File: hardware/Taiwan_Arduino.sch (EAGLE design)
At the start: 43 parts, among them J1 AVR_SPI_PRG_62X3_LOCK, T2 2N2222, U1 ATMEGA328P_PDIP, U2 SPI_FLASH, Y2 16mhz

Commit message: add FTDI Tag
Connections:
- net GND: now also S1.2; no longer S1.1
- net RST: now also S1.1; no longer S1.2
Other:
- moved on the sheet: S1
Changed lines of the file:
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@@
 <?xml version="1.0" encoding="utf-8"?>
 <!DOCTYPE eagle SYSTEM "eagle.dtd">
-<eagle version="7.2.0">
+<eagle version="7.4.0">
 <drawing>
 <settings>
@@
 <grid distance="0.1" unitdist="inch" unit="inch" style="lines" multiple="1" display="no" altdistance="0.01" altunitdist="inch" altunit="inch"/>
 <layers>
-<layer number="1" name="Top" color="4" fill="1" visible="yes" active="no"/>
-<layer number="16" name="Bottom" color="1" fill="1" visible="yes" active="no"/>
-<layer number="17" name="Pads" color="2" fill="1" visible="yes" active="no"/>
-<layer number="18" name="Vias" color="2" fill="1" visible="yes" active="no"/>
-<layer number="19" name="Unrouted" color="6" fill="1" visible="yes" active="no"/>
-<layer number="20" name="Dimension" color="15" fill="1" visible="yes" active="no"/>
-<layer number="21" name="tPlace" color="7" fill="1" visible="yes" active="no"/>
-<layer number="22" name="bPlace" color="7" fill="1" visible="yes" active="no"/>
-<layer number="23" name="tOrigins" color="15" fill="1" visible="yes" active="no"/>
-<layer number="24" name="bOrigins" color="15" fill="1" visible="yes" active="no"/>
-<layer number="25" name="tNames" color="7" fill="1" visible="yes" active="no"/>
-<layer number="26" name="bNames" color="7" fill="1" visible="yes" active="no"/>
-<layer number="27" name="tValues" color="7" fill="1" visible="yes" active="no"/>
-<layer number="28" name="bValues" color="7" fill="1" visible="yes" active="no"/>
+<layer number="1" name="Top" color="4" fill="1" visible="no" active="no"/>
+<layer number="16" name="Bottom" color="1" fill="1" visible="no" active="no"/>
+<layer number="17" name="Pads" color="2" fill="1" visible="no" active="no"/>
+<layer number="18" name="Vias" color="2" fill="1" visible="no" active="no"/>
+<layer number="19" name="Unrouted" color="6" fill="1" visible="no" active="no"/>
+<layer number="20" name="Dimension" color="15" fill="1" visible="no" active="no"/>
+<layer number="21" name="tPlace" color="7" fill="1" visible="no" active="no"/>
+<layer number="22" name="bPlace" color="7" fill="1" visible="no" active="no"/>
+<layer number="23" name="tOrigins" color="15" fill="1" visible="no" active="no"/>
+<layer number="24" name="bOrigins" color="15" fill="1" visible="no" active="no"/>
+<layer number="25" name="tNames" color="7" fill="1" visible="no" active="no"/>
+<layer number="26" name="bNames" color="7" fill="1" visible="no" active="no"/>
+<layer number="27" name="tValues" color="7" fill="1" visible="no" active="no"/>
+<layer number="28" name="bValues" color="7" fill="1" visible="no" active="no"/>
 <layer number="29" name="tStop" color="7" fill="3" visible="no" active="no"/>
 <layer number="30" name="bStop" color="7" fill="6" visible="no" active="no"/>
@@
 <layer number="35" name="tGlue" color="7" fill="4" visible="no" active="no"/>
 <layer number="36" name="bGlue" color="7" fill="5" visible="no" active="no"/>
-<layer number="37" name="tTest" color="7" fill="1" visible="yes" active="no"/>
-<layer number="38" name="bTest" color="7" fill="1" visible="yes" active="no"/>
+<layer number="37" name="tTest" color="7" fill="1" visible="no" active="no"/>
+<layer number="38" name="bTest" color="7" fill="1" visible="no" active="no"/>
 <layer number="39" name="tKeepout" color="4" fill="11" visible="no" active="no"/>
 <layer number="40" name="bKeepout" color="1" fill="11" visible="no" active="no"/>
@@
 <layer number="44" name="Drills" color="7" fill="1" visible="no" active="no"/>
 <layer number="45" name="Holes" color="7" fill="1" visible="no" active="no"/>
-<layer number="46" name="Milling" color="3" fill="1" visible="yes" active="no"/>
-<layer number="47" name="Measures" color="7" fill="1" visible="yes" active="no"/>
-<layer number="48" name="Document" color="7" fill="1" visible="yes" active="no"/>
-<layer number="49" name="Reference" color="7" fill="1" visible="yes" active="no"/>
-<layer number="50" name="dxf" color="7" fill="1" visible="yes" active="no"/>
-<layer number="51" name="tDocu" color="7" fill="1" visible="yes" active="no"/>
-<layer number="52" name="bDocu" color="7" fill="1" visible="yes" active="no"/>
-<layer number="53" name="tGND_GNDA" color="7" fill="9" visible="yes" active="no"/>
-<layer number="54" name="bGND_GNDA" color="1" fill="9" visible="yes" active="no"/>
-<layer number="56" name="wert" color="7" fill="1" visible="yes" active="no"/>
-<layer number="57" name="tCAD" color="7" fill="1" visible="yes" active="no"/>
-<layer number="59" name="tCarbon" color="7" fill="1" visible="yes" active="no"/>
-<layer number="60" name="bCarbon" color="7" fill="1" visible="yes" active="no"/>
+<layer number="46" name="Milling" color="3" fill="1" visible="no" active="no"/>
+<layer number="47" name="Measures" color="7" fill="1" visible="no" active="no"/>
+<layer number="48" name="Document" color="7" fill="1" visible="no" active="no"/>
+<layer number="49" name="Reference" color="7" fill="1" visible="no" active="no"/>
+<layer number="50" name="dxf" color="7" fill="1" visible="no" active="no"/>
+<layer number="51" name="tDocu" color="7" fill="1" visible="no" active="no"/>
+<layer number="52" name="bDocu" color="7" fill="1" visible="no" active="no"/>
+<layer number="53" name="tGND_GNDA" color="7" fill="9" visible="no" active="no"/>
+<layer number="54" name="bGND_GNDA" color="1" fill="9" visible="no" active="no"/>
+<layer number="56" name="wert" color="7" fill="1" visible="no" active="no"/>
+<layer number="57" name="tCAD" color="7" fill="1" visible="no" active="no"/>
+<layer number="59" name="tCarbon" color="7" fill="1" visible="no" active="no"/>
+<layer number="60" name="bCarbon" color="7" fill="1" visible="no" active="no"/>
 <layer number="90" name="Modules" color="5" fill="1" visible="yes" active="yes"/>
 <layer number="91" name="Nets" color="2" fill="1" visible="yes" active="yes"/>
@@
 <attribute name="VALUE" x="88.9" y="30.48" size="1.27" layer="96"/>
 </instance>
-<instance part="S1" gate="G$1" x="43.18" y="139.7" smashed="yes" rot="R180">
-<attribute name="NAME" x="43.18" y="142.24" size="1.778" layer="95" rot="R180"/>
-</instance>
-<instance part="GND7" gate="1" x="55.88" y="137.16"/>
+<instance part="S1" gate="G$1" x="43.18" y="139.7" smashed="yes">
+<attribute name="NAME" x="43.18" y="137.16" size="1.778" layer="95"/>
+</instance>
+<instance part="GND7" gate="1" x="48.26" y="137.16"/>
 <instance part="D1" gate="G$1" x="76.2" y="66.04" rot="R270"/>
 <instance part="R3" gate="G$1" x="66.04" y="66.04" rot="R180"/>
@@
 </segment>
 <segment>
-<pinref part="S1" gate="G$1" pin="1"/>
-<pinref part="GND7" gate="1" pin="GND"/>
-<wire x1="55.88" y1="139.7" x2="48.26" y2="139.7" width="0.1524" layer="91"/>
-</segment>
-<segment>
 <pinref part="GND12" gate="1" pin="GND"/>
 <pinref part="D5" gate="1" pin="A"/>
@@
 <pinref part="JP1" gate="G$1" pin="1"/>
 <wire x1="180.34" y1="81.28" x2="180.34" y2="73.66" width="0.1524" layer="91"/>
+</segment>
+<segment>
+<pinref part="S1" gate="G$1" pin="2"/>
+<pinref part="GND7" gate="1" pin="GND"/>
 </segment>
 </net>
@@
 <wire x1="38.1" y1="147.32" x2="139.7" y2="147.32" width="0.1524" layer="91"/>
 <wire x1="139.7" y1="147.32" x2="139.7" y2="116.84" width="0.1524" layer="91"/>
-<pinref part="S1" gate="G$1" pin="2"/>
 <wire x1="38.1" y1="147.32" x2="38.1" y2="139.7" width="0.1524" layer="91"/>
 <pinref part="U1" gate="G$1" pin="PC6(/RESET)"/>
@@
 <wire x1="38.1" y1="139.7" x2="38.1" y2="132.08" width="0.1524" layer="91"/>
 <wire x1="38.1" y1="139.7" x2="12.7" y2="139.7" width="0.1524" layer="91"/>
-</segment>
-</net>
+<pinref part="S1" gate="G$1" pin="1"/>
+<junction x="38.1" y="139.7"/>
+</segment>
+</net>

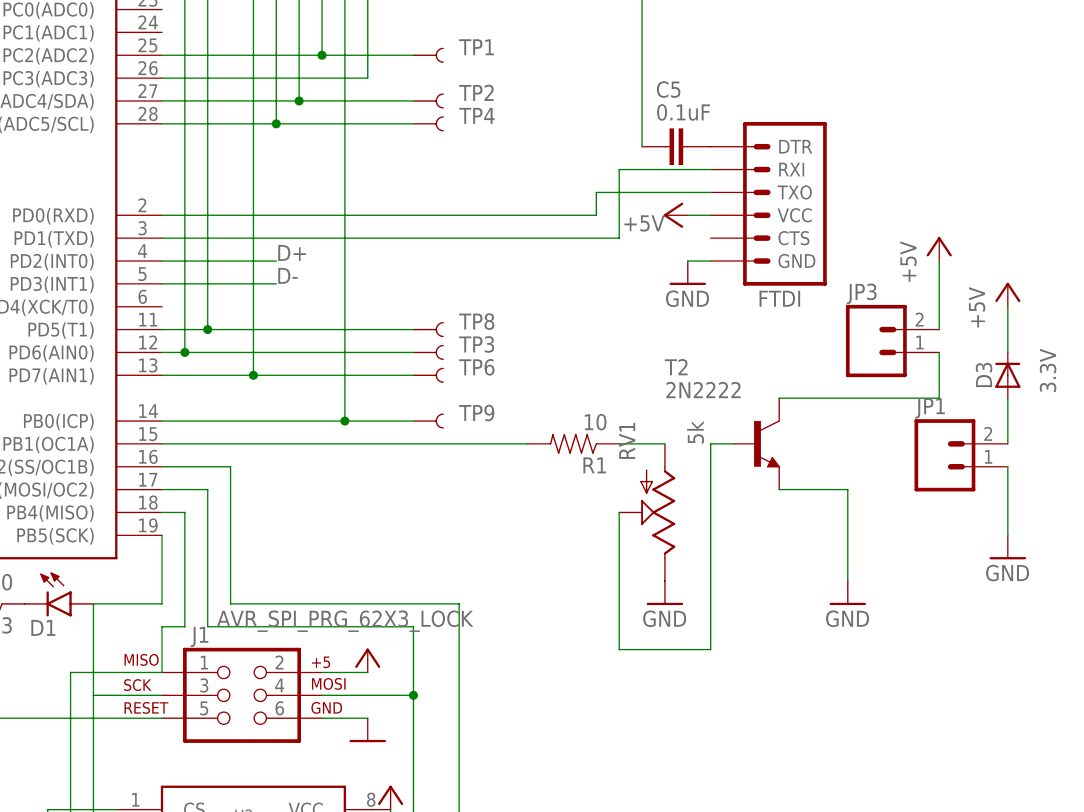
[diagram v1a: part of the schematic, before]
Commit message: Fix 10 ohm R1
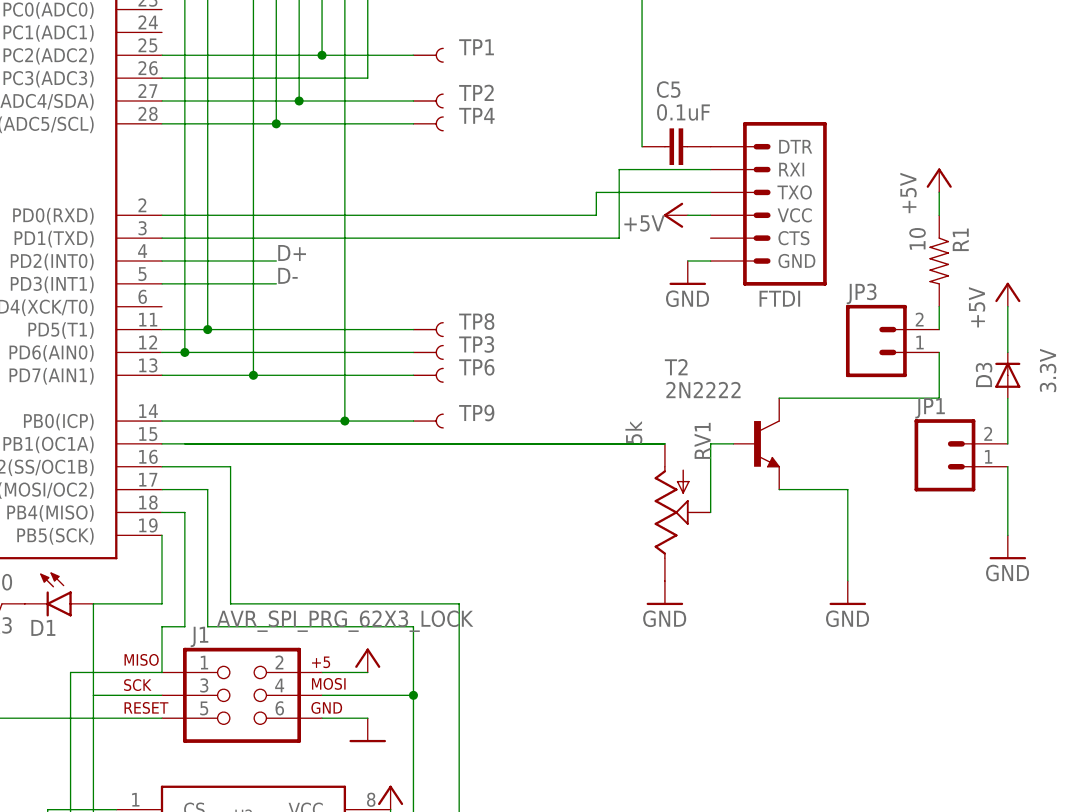
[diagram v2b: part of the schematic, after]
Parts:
- R1: device SparkFun-Resistors:RESISTORPTH-1/4W -> SparkFun-Resistors:RESISTORPTH-1/4W-VERT
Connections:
- net +5V: now also R1.1; no longer JP3.2
- net N$1: now also JP3.2, R1.2; no longer R1.1, RV1.A
- net N$2: now also RV1.A; no longer R1.2
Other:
- moved on the sheet: R1, RV1
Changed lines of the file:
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@@
 <?xml version="1.0" encoding="utf-8"?>
 <!DOCTYPE eagle SYSTEM "eagle.dtd">
-<eagle version="7.4.0">
+<eagle version="7.2.0">
 <drawing>
 <settings>
@@
 <grid distance="0.1" unitdist="inch" unit="inch" style="lines" multiple="1" display="no" altdistance="0.01" altunitdist="inch" altunit="inch"/>
 <layers>
-<layer number="1" name="Top" color="4" fill="1" visible="no" active="no"/>
-<layer number="16" name="Bottom" color="1" fill="1" visible="no" active="no"/>
-<layer number="17" name="Pads" color="2" fill="1" visible="no" active="no"/>
-<layer number="18" name="Vias" color="2" fill="1" visible="no" active="no"/>
-<layer number="19" name="Unrouted" color="6" fill="1" visible="no" active="no"/>
-<layer number="20" name="Dimension" color="15" fill="1" visible="no" active="no"/>
-<layer number="21" name="tPlace" color="7" fill="1" visible="no" active="no"/>
-<layer number="22" name="bPlace" color="7" fill="1" visible="no" active="no"/>
-<layer number="23" name="tOrigins" color="15" fill="1" visible="no" active="no"/>
-<layer number="24" name="bOrigins" color="15" fill="1" visible="no" active="no"/>
-<layer number="25" name="tNames" color="7" fill="1" visible="no" active="no"/>
-<layer number="26" name="bNames" color="7" fill="1" visible="no" active="no"/>
-<layer number="27" name="tValues" color="7" fill="1" visible="no" active="no"/>
-<layer number="28" name="bValues" color="7" fill="1" visible="no" active="no"/>
+<layer number="1" name="Top" color="4" fill="1" visible="yes" active="no"/>
+<layer number="16" name="Bottom" color="1" fill="1" visible="yes" active="no"/>
+<layer number="17" name="Pads" color="2" fill="1" visible="yes" active="no"/>
+<layer number="18" name="Vias" color="2" fill="1" visible="yes" active="no"/>
+<layer number="19" name="Unrouted" color="6" fill="1" visible="yes" active="no"/>
+<layer number="20" name="Dimension" color="15" fill="1" visible="yes" active="no"/>
+<layer number="21" name="tPlace" color="7" fill="1" visible="yes" active="no"/>
+<layer number="22" name="bPlace" color="7" fill="1" visible="yes" active="no"/>
+<layer number="23" name="tOrigins" color="15" fill="1" visible="yes" active="no"/>
+<layer number="24" name="bOrigins" color="15" fill="1" visible="yes" active="no"/>
+<layer number="25" name="tNames" color="7" fill="1" visible="yes" active="no"/>
+<layer number="26" name="bNames" color="7" fill="1" visible="yes" active="no"/>
+<layer number="27" name="tValues" color="7" fill="1" visible="yes" active="no"/>
+<layer number="28" name="bValues" color="7" fill="1" visible="yes" active="no"/>
 <layer number="29" name="tStop" color="7" fill="3" visible="no" active="no"/>
 <layer number="30" name="bStop" color="7" fill="6" visible="no" active="no"/>
@@
 <layer number="35" name="tGlue" color="7" fill="4" visible="no" active="no"/>
 <layer number="36" name="bGlue" color="7" fill="5" visible="no" active="no"/>
-<layer number="37" name="tTest" color="7" fill="1" visible="no" active="no"/>
-<layer number="38" name="bTest" color="7" fill="1" visible="no" active="no"/>
+<layer number="37" name="tTest" color="7" fill="1" visible="yes" active="no"/>
+<layer number="38" name="bTest" color="7" fill="1" visible="yes" active="no"/>
 <layer number="39" name="tKeepout" color="4" fill="11" visible="no" active="no"/>
 <layer number="40" name="bKeepout" color="1" fill="11" visible="no" active="no"/>
@@
 <layer number="44" name="Drills" color="7" fill="1" visible="no" active="no"/>
 <layer number="45" name="Holes" color="7" fill="1" visible="no" active="no"/>
-<layer number="46" name="Milling" color="3" fill="1" visible="no" active="no"/>
-<layer number="47" name="Measures" color="7" fill="1" visible="no" active="no"/>
-<layer number="48" name="Document" color="7" fill="1" visible="no" active="no"/>
-<layer number="49" name="Reference" color="7" fill="1" visible="no" active="no"/>
-<layer number="50" name="dxf" color="7" fill="1" visible="no" active="no"/>
-<layer number="51" name="tDocu" color="7" fill="1" visible="no" active="no"/>
-<layer number="52" name="bDocu" color="7" fill="1" visible="no" active="no"/>
-<layer number="53" name="tGND_GNDA" color="7" fill="9" visible="no" active="no"/>
-<layer number="54" name="bGND_GNDA" color="1" fill="9" visible="no" active="no"/>
-<layer number="56" name="wert" color="7" fill="1" visible="no" active="no"/>
-<layer number="57" name="tCAD" color="7" fill="1" visible="no" active="no"/>
-<layer number="59" name="tCarbon" color="7" fill="1" visible="no" active="no"/>
-<layer number="60" name="bCarbon" color="7" fill="1" visible="no" active="no"/>
+<layer number="46" name="Milling" color="3" fill="1" visible="yes" active="no"/>
+<layer number="47" name="Measures" color="7" fill="1" visible="yes" active="no"/>
+<layer number="48" name="Document" color="7" fill="1" visible="yes" active="no"/>
+<layer number="49" name="Reference" color="7" fill="1" visible="yes" active="no"/>
+<layer number="50" name="dxf" color="7" fill="1" visible="yes" active="no"/>
+<layer number="51" name="tDocu" color="7" fill="1" visible="yes" active="no"/>
+<layer number="52" name="bDocu" color="7" fill="1" visible="yes" active="no"/>
+<layer number="53" name="tGND_GNDA" color="7" fill="9" visible="yes" active="no"/>
+<layer number="54" name="bGND_GNDA" color="1" fill="9" visible="yes" active="no"/>
+<layer number="56" name="wert" color="7" fill="1" visible="yes" active="no"/>
+<layer number="57" name="tCAD" color="7" fill="1" visible="yes" active="no"/>
+<layer number="59" name="tCarbon" color="7" fill="1" visible="yes" active="no"/>
+<layer number="60" name="bCarbon" color="7" fill="1" visible="yes" active="no"/>
 <layer number="90" name="Modules" color="5" fill="1" visible="yes" active="yes"/>
 <layer number="91" name="Nets" color="2" fill="1" visible="yes" active="yes"/>
@@
 <part name="GND16" library="supply1" deviceset="GND" device=""/>
 <part name="P+6" library="supply1" deviceset="+5V" device=""/>
-<part name="R1" library="SparkFun-Resistors" deviceset="RESISTOR" device="PTH-1/4W" value="10"/>
+<part name="R1" library="SparkFun-Resistors" deviceset="RESISTOR" device="PTH-1/4W-VERT" value="10"/>
 <part name="TP3" library="SparkFun-Passives" deviceset="TEST-POINT" device=""/>
 <part name="TP1" library="SparkFun-Passives" deviceset="TEST-POINT" device=""/>
@@
 <instance part="GND16" gate="1" x="109.22" y="50.8" smashed="yes"/>
 <instance part="P+6" gate="1" x="109.22" y="60.96" smashed="yes"/>
-<instance part="R1" gate="G$1" x="132.08" y="83.82" rot="R180"/>
+<instance part="R1" gate="G$1" x="172.72" y="104.14" rot="R270"/>
 <instance part="TP3" gate="G$1" x="114.3" y="93.98" smashed="yes">
 <attribute name="NAME" x="119.38" y="93.98" size="1.778" layer="95"/>
@@
 <instance part="FTDI" gate="G$1" x="152.4" y="111.76" rot="R180"/>
 <instance part="GND3" gate="1" x="162.56" y="66.04"/>
-<instance part="P+1" gate="1" x="172.72" y="106.68"/>
-<instance part="RV1" gate="G$1" x="142.24" y="76.2" rot="R180"/>
+<instance part="P+1" gate="1" x="172.72" y="114.3"/>
+<instance part="RV1" gate="G$1" x="142.24" y="76.2" rot="MR180"/>
 <instance part="GND6" gate="1" x="142.24" y="66.04"/>
 <instance part="U2" gate="G$1" x="96.52" y="40.64" smashed="yes">
@@
 </segment>
 <segment>
-<pinref part="P+1" gate="1" pin="+5V"/>
-<wire x1="172.72" y1="104.14" x2="172.72" y2="96.52" width="0.1524" layer="91"/>
-<pinref part="JP3" gate="G$1" pin="2"/>
-</segment>
-<segment>
 <pinref part="D3" gate="1" pin="C"/>
 <pinref part="P+9" gate="1" pin="+5V"/>
 <wire x1="180.34" y1="93.98" x2="180.34" y2="99.06" width="0.1524" layer="91"/>
+</segment>
+<segment>
+<pinref part="P+1" gate="1" pin="+5V"/>
+<pinref part="R1" gate="G$1" pin="1"/>
+<wire x1="172.72" y1="111.76" x2="172.72" y2="109.22" width="0.1524" layer="91"/>
 </segment>
 </net>
@@
 </segment>
 </net>
-<net name="N$2" class="0">
-<segment>
-<pinref part="U1" gate="G$1" pin="PB1(OC1A)"/>
-<pinref part="R1" gate="G$1" pin="2"/>
-<wire x1="86.36" y1="83.82" x2="127" y2="83.82" width="0.1524" layer="91"/>
-</segment>
-</net>
 <net name="N$3" class="0">
 <segment>
@@
 <pinref part="T2" gate="G$1" pin="B"/>
 <wire x1="149.86" y1="83.82" x2="147.32" y2="83.82" width="0.1524" layer="91"/>
-<wire x1="147.32" y1="83.82" x2="147.32" y2="60.96" width="0.1524" layer="91"/>
+<wire x1="147.32" y1="83.82" x2="147.32" y2="76.2" width="0.1524" layer="91"/>
 <pinref part="RV1" gate="G$1" pin="S"/>
-<wire x1="147.32" y1="60.96" x2="137.16" y2="60.96" width="0.1524" layer="91"/>
-<wire x1="137.16" y1="60.96" x2="137.16" y2="76.2" width="0.1524" layer="91"/>
 </segment>
 </net>
@@
 </segment>
 </net>
-<net name="N$1" class="0">
-<segment>
-<pinref part="R1" gate="G$1" pin="1"/>
-<pinref part="RV1" gate="G$1" pin="A"/>
-<wire x1="142.24" y1="83.82" x2="137.16" y2="83.82" width="0.1524" layer="91"/>
-</segment>
-</net>
 <net name="N$12" class="0">
 <segment>
@@
 </segment>
 </net>
+<net name="N$1" class="0">
+<segment>
+<pinref part="JP3" gate="G$1" pin="2"/>
+<pinref part="R1" gate="G$1" pin="2"/>
+<wire x1="172.72" y1="99.06" x2="172.72" y2="96.52" width="0.1524" layer="91"/>
+</segment>
+</net>
+<net name="N$2" class="0">
+<segment>
+<pinref part="RV1" gate="G$1" pin="A"/>
+<wire x1="88.9" y1="83.82" x2="142.24" y2="83.82" width="0.1524" layer="91"/>
+<pinref part="U1" gate="G$1" pin="PB1(OC1A)"/>
+<wire x1="142.24" y1="83.82" x2="86.36" y2="83.82" width="0.1524" layer="91"/>
+</segment>
+</net>
